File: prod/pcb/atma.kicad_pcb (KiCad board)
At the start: 2 copper layers, 114.1 x 81 mm, 25 parts

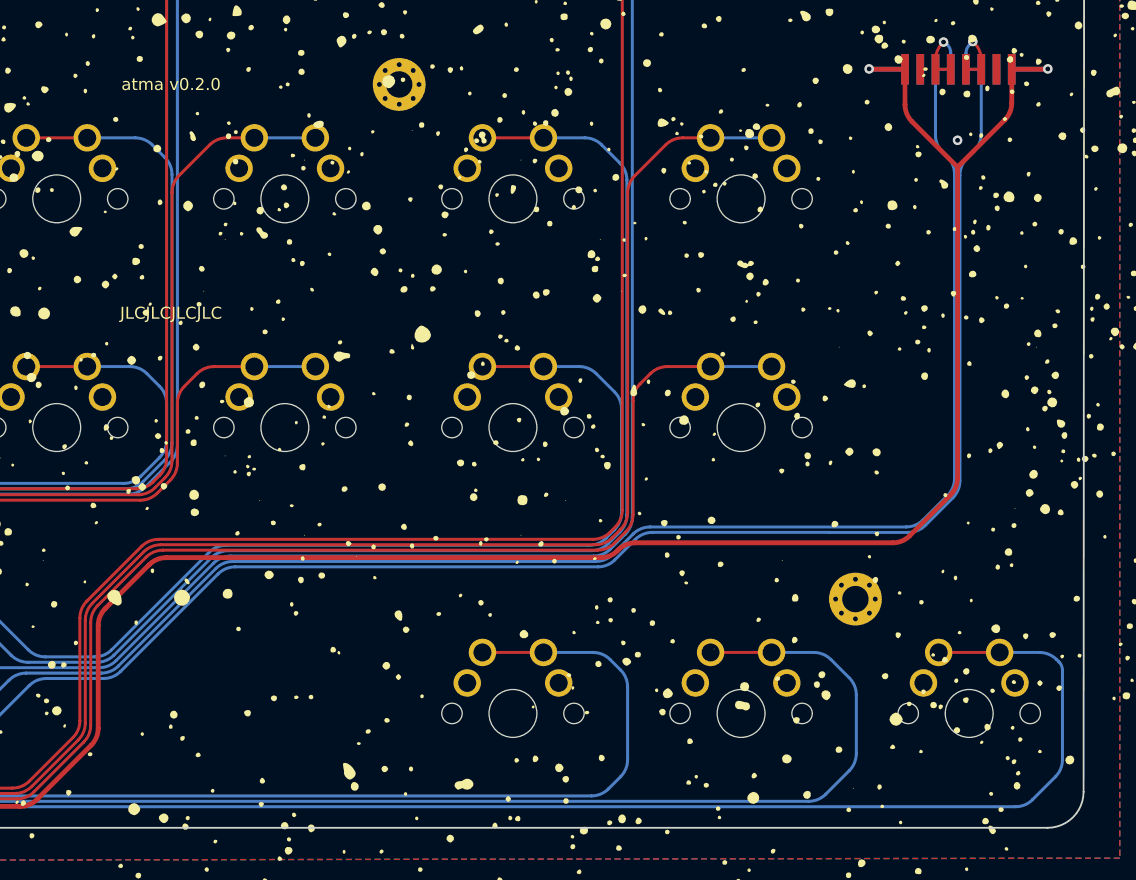
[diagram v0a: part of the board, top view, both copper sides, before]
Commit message: drop the outer thumb a few mm
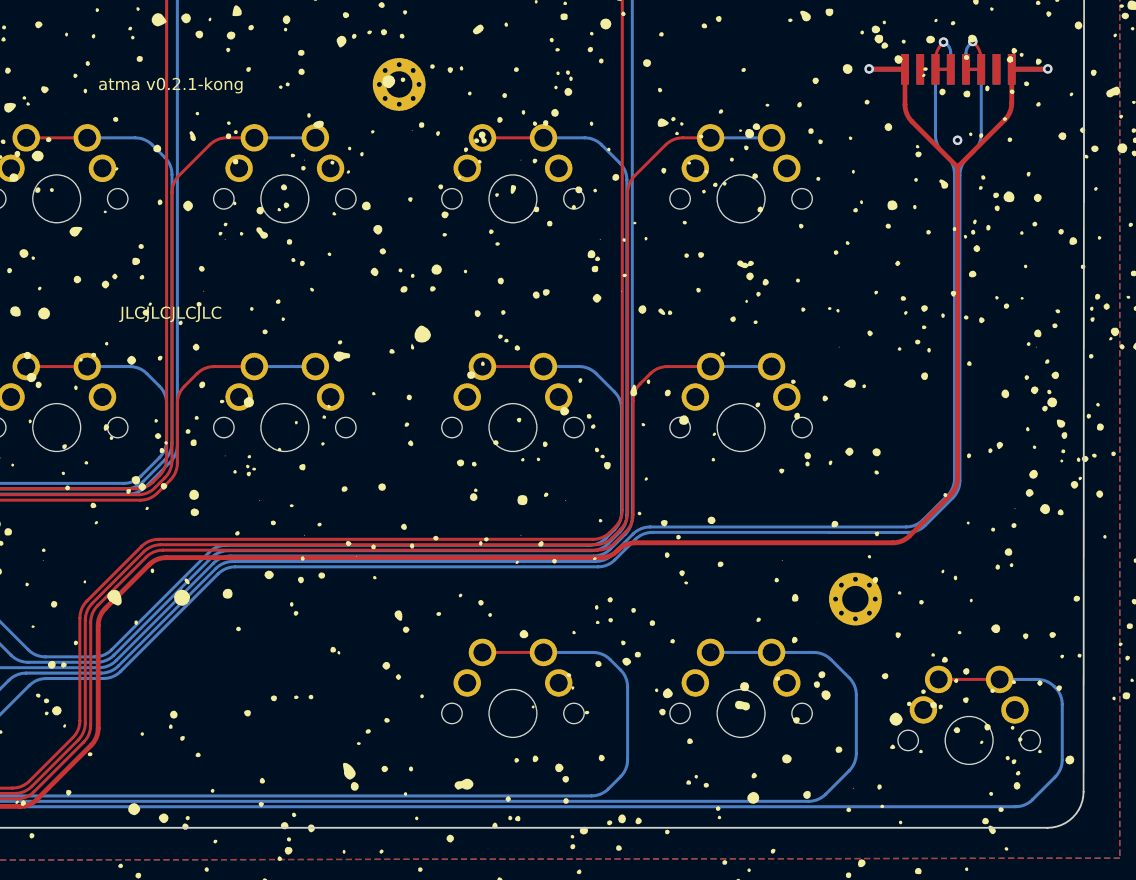
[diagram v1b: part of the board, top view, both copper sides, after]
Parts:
- moved S18 2.25 mm to (247.4, 178.5)
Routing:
- net thumbfan_far_home: track 124.7 -> 122.3 mm
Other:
- board text added: "atma v0.2.1-kong"
- board text removed: "atma v0.2.0"
